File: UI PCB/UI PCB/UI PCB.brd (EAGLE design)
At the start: 160 x 100 mm, 23 parts, among them IC1 MCP23S17SP, IC2 MCP23S17SP, X1 JST-XH-02-PIN-ROUND-PAD, X2 JST-XH-02-PIN-ROUND-PAD, X3 JST-XH-02-PIN-ROUND-PAD, X4 JST-XH-02-PIN-ROUND-PAD, X5 JST-XH-05-PIN-ROUND-PAD, X6 JST-XH-05-PIN-ROUND-PAD, X7 JST-XH-05-PIN-ROUND-PAD, X8 JST-XH-05-PIN-ROUND-PAD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

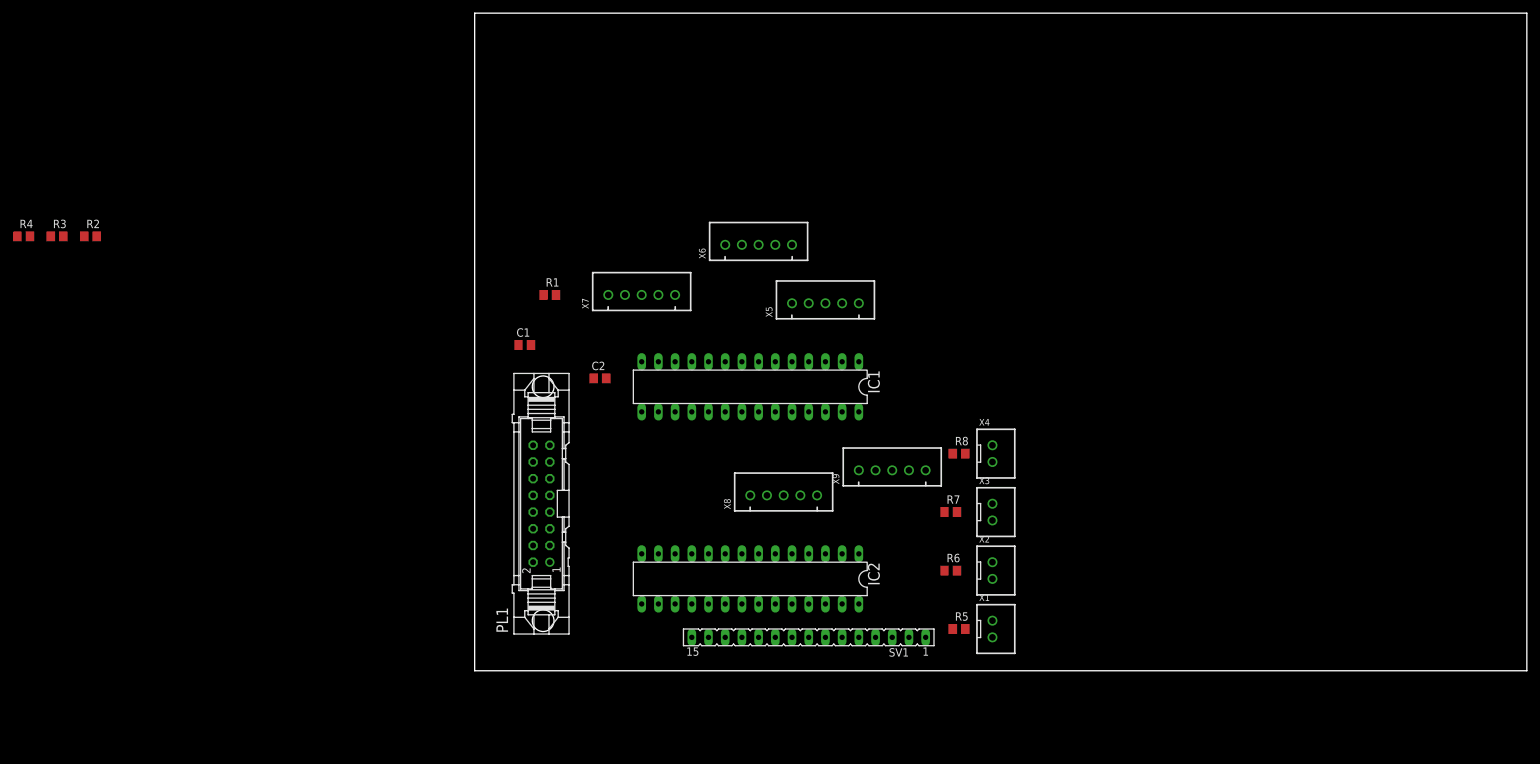
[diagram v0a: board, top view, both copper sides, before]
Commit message: added libraries and a part of the PCB design
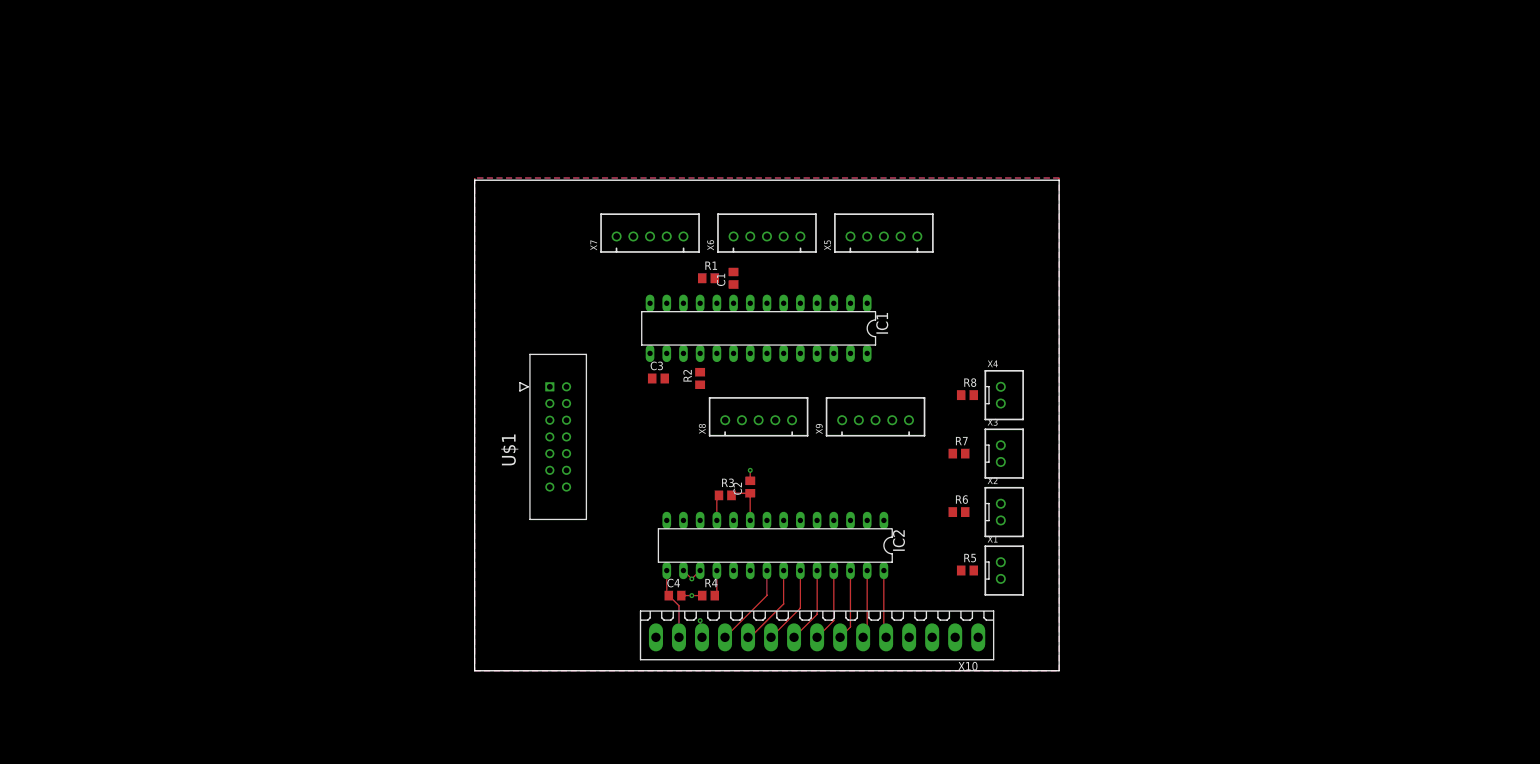
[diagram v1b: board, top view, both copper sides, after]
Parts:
- removed PL1: (no value), con-harting-v:16V
- removed SV1: (no value), con-lsta:FE15
- added C3, C4: (no value), rcl:C0805
- added U$1: 2514-6002UB, 2514-6002UB:3M_2514-6002UB
- added X10: (no value), con-weidmueller-sl35:180G-15
- moved R4 117.6 mm to (35.6, 11.4)
- moved R3 109.0 mm to (38.1, 26.7)
- moved R2 95.2 mm to (34.3, 44.5), turned to 90 degrees
- moved C1 33.3 mm to (39.4, 59.7), turned to 90 degrees
- moved C2 28.2 mm to (41.9, 27.9), turned to 90 degrees
- moved R1 24.3 mm to (35.6, 59.7)
- moved X5 13.5 mm to (62.2, 66.0)
- moved X8 12.0 mm to (43.2, 38.1)
- moved X7 8.98 mm to (26.7, 66.0)
- moved X3 8.98 mm to (80.0, 33.0)
- moved R7 8.98 mm to (73.7, 33.0)
- moved IC1 8.98 mm to (43.2, 52.1)
- moved R5 8.98 mm to (74.9, 15.2)
- moved X1 8.98 mm to (80.0, 15.2)
- moved X2 8.98 mm to (80.0, 24.1)
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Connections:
- removed net A0: IC1.15, IC2.15, PL1.5
- removed net A1: IC1.16, IC2.16, PL1.6
- removed net CLK: PL1.7
- removed net N$16: PL1.16
- new net N$1: U$1.1
- new net N$10: U$1.6
- new net N$11: U$1.8
- new net N$12: U$1.10
- new net N$13: U$1.12
- new net N$14: U$1.14
- new net N$2: U$1.3
- new net N$3: U$1.5
- new net N$4: U$1.7
- new net N$5: U$1.9
- new net N$6: U$1.11
- new net N$7: U$1.13
- new net N$8: U$1.2
- new net N$9: U$1.4
- net 3V3: now also C3.1, C4.1, IC2.15, X10.14; no longer PL1.13, SV1.14
- net 5V: now also X10.15; no longer PL1.14, SV1.15
- net CS1: no longer PL1.10
- net CS2: no longer PL1.11
- net GND: now also C3.2, C4.2, IC1.15, IC1.16, IC1.17, IC2.16, IC2.17, X10.13; no longer PL1.15, SV1.13
- net GPA0: now also X10.12; no longer SV1.12
- net GPA1: now also X10.11; no longer SV1.11
- net GPA2: now also X10.10; no longer SV1.10
- net GPA3: now also X10.9; no longer SV1.9
- net GPA4: now also X10.8; no longer SV1.8
- net GPA5: now also X10.7; no longer SV1.7
- net GPA6: now also X10.6; no longer SV1.6
- net GPA7: now also X10.5; no longer SV1.5
- net GPB4: now also X10.4; no longer SV1.4
- net GPB5: now also X10.3; no longer SV1.3
- net GPB6: now also X10.2; no longer SV1.2
- net GPB7: now also X10.1; no longer SV1.1
- net INTA1: no longer PL1.1
- net INTA2: no longer PL1.3
- net INTB1: no longer PL1.2
- net INTB2: no longer PL1.4
- net MISO: no longer PL1.8
- net MOSI: no longer PL1.9
- net RESET: no longer PL1.12
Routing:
- net 3V3: track 0.00 -> 18.1 mm
- net GPA0: track 0.00 -> 12.8 mm
- net GPA1: track 0.00 -> 12.3 mm
- net GPA2: track 0.00 -> 12.0 mm
- net GPA3: track 0.00 -> 11.6 mm
- net GPA4: track 0.00 -> 11.2 mm
- net GND: track 0.00 -> 11.0 mm, vias 0 -> 4
- net GPA5: track 0.00 -> 10.8 mm
- net GPA6: track 0.00 -> 10.4 mm
- net GPA7: track 0.00 -> 10.3 mm
- net CS2: track 0.00 -> 3.94 mm
- net RESET: track 0.00 -> 3.94 mm
- added copper zone on layer 1, net GND
- added copper zone on layer 16, net GND
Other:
- board size 160 x 100 mm -> 88.9 x 74.6 mm

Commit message: improve the schemetic on the io expanders and add the right header for the stm32 connection
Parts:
- removed C3, C4: (no value), rcl:C0805
- moved C1 77.9 mm to (7.62, -11.4), turned to 0 degrees
- moved R1 72.7 mm to (2.54, -5.08)
- moved R2 64.3 mm to (2.54, -11.4), turned to 0 degrees
- moved X8 3.81 mm to (43.2, 34.3)
- moved X9 3.81 mm to (61.0, 34.3)
- moved IC1 3.59 mm to (45.7, 49.5)
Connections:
- net N$1 renamed OPEN
- removed net N$10: U$1.6
- removed net N$11: U$1.8
- removed net N$12: U$1.10
- removed net N$13: U$1.12
- removed net N$14: U$1.14
- removed net N$2: U$1.3
- removed net N$3: U$1.5
- removed net N$4: U$1.7
- removed net N$5: U$1.9
- removed net N$6: U$1.11
- removed net N$7: U$1.13
- removed net N$8: U$1.2
- removed net N$9: U$1.4
- removed net SCK: IC1.12, IC2.12
- new net CLK: IC1.12, IC2.12, U$1.14
- net 3V3: now also U$1.4; no longer C3.1, C4.1, R1.2, R3.2
- net 5V: now also U$1.3
- net CS1: now also R1.2, U$1.11; no longer R1.1
- net CS2: now also R3.2, U$1.10; no longer R3.1
- net GND: now also R1.1, R3.1, U$1.2; no longer C3.2, C4.2
- net INTA1: now also U$1.8
- net INTA2: now also U$1.5
- net INTB1: now also U$1.7
- net INTB2: now also U$1.6
- net MISO: now also U$1.13
- net MOSI: now also U$1.12
- net RESET: now also U$1.9
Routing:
- net ROTARY_ENC_5_B: track 0.00 -> 20.5 mm
- net 3V3: track 18.1 -> 37.5 mm
- net ROTARY_ENC_4_BUTTON: track 0.00 -> 18.0 mm
- net ROTARY_ENC_4_A: track 0.00 -> 15.1 mm
- net ROTARY_ENC_5_BUTTON: track 0.00 -> 13.0 mm
- net ROTARY_ENC_5_A: track 0.00 -> 12.0 mm
- net ROTARY_ENC_4_B: track 0.00 -> 12.0 mm
- net CS2: track 3.94 -> 0.00 mm
- net GND: track 11.0 -> 9.43 mm
- net GPA1: track 12.3 -> 11.0 mm

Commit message: redesigned PCB
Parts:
- removed X10: (no value), con-weidmueller-sl35:180G-15
- added J1: (no value), SparkFun-Connectors:1X15
- moved X5 42.8 mm to (25.1, 44.7)
- moved X6 41.9 mm to (8.38, 44.7)
- moved X7 40.2 mm to (3.05, 33.5), turned to 270 degrees
- moved IC1 38.7 mm to (20.3, 20.3), turned to 270 degrees
- moved R2 32.4 mm to (26.7, 10.2), turned to 90 degrees
- moved C1 28.4 mm to (12.7, 16.5), turned to 180 degrees
- moved U$1 24.1 mm to (6.35, 20.3)
- moved X9 21.7 mm to (41.9, 44.7)
- moved R5 19.4 mm to (58.4, 5.08), turned to 90 degrees
- moved X1 19.4 mm to (63.5, 5.08), turned to 90 degrees
- moved R1 19.4 mm to (12.7, 11.4)
- moved X2 18.8 mm to (63.5, 15.2), turned to 90 degrees
- moved X8 18.7 mm to (58.7, 44.7)
- moved X3 18.2 mm to (63.5, 25.4), turned to 90 degrees
- moved R8 17.7 mm to (58.4, 35.6), turned to 90 degrees
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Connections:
- net 3V3: now also J1.14, X5.2, X6.2, X7.2, X8.2, X9.2; no longer X10.14, X5.3, X6.3, X7.3, X8.3, X9.3
- net 5V: now also J1.15; no longer X10.15
- net GND: now also J1.13, X5.1, X6.1, X7.1, X8.1, X9.1; no longer X10.13, X5.2, X6.2, X7.2, X8.2, X9.2
- net GPA0: now also J1.12; no longer X10.12
- net GPA1: now also J1.11; no longer X10.11
- net GPA2: now also J1.10; no longer X10.10
- net GPA3: now also J1.9; no longer X10.9
- net GPA4: now also J1.8; no longer X10.8
- net GPA5: now also J1.7; no longer X10.7
- net GPA6: now also J1.6; no longer X10.6
- net GPA7: now also J1.5; no longer X10.5
- net GPB4: now also J1.4; no longer X10.4
- net GPB5: now also J1.3; no longer X10.3
- net GPB6: now also J1.2; no longer X10.2
- net GPB7: now also J1.1; no longer X10.1
- net ROTARY_ENC_1_A: now also X5.5; no longer X5.1
- net ROTARY_ENC_1_B: now also X5.4; no longer X5.5
- net ROTARY_ENC_1_BUTTON: now also X5.3; no longer X5.4
- net ROTARY_ENC_2_A: now also X6.5; no longer X6.1
- net ROTARY_ENC_2_B: now also X6.4; no longer X6.5
- net ROTARY_ENC_2_BUTTON: now also X6.3; no longer X6.4
- net ROTARY_ENC_3_A: now also IC1.8, X7.5; no longer IC1.7, X7.1
- net ROTARY_ENC_3_B: now also IC1.7, X7.4; no longer IC1.8, X7.5
- net ROTARY_ENC_3_BUTTON: now also X7.3; no longer X7.4
- net ROTARY_ENC_4_A: now also X8.5; no longer X8.1
- net ROTARY_ENC_4_B: now also X8.4; no longer X8.5
- net ROTARY_ENC_4_BUTTON: now also X8.3; no longer X8.4
- net ROTARY_ENC_5_A: now also X9.5; no longer X9.1
- net ROTARY_ENC_5_B: now also X9.4; no longer X9.5
- net ROTARY_ENC_5_BUTTON: now also X9.3; no longer X9.4
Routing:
- net 3V3: track 37.5 -> 191.2 mm, vias 0 -> 2
- net 5V: track 0.00 -> 65.2 mm
- net CS1_BUTTON: track 0.00 -> 62.7 mm
- net CS2_BUTTON: track 0.00 -> 57.8 mm
- net CS3_BUTTON: track 0.00 -> 51.2 mm
- net CS4_BUTTON: track 0.00 -> 44.7 mm
- net INTA2: track 0.00 -> 41.7 mm, vias 0 -> 1
- net RESET: track 3.94 -> 44.9 mm
- net ROTARY_ENC_4_A: track 15.1 -> 55.3 mm
- net INTB2: track 0.00 -> 39.8 mm
- net GPB4: track 0.00 -> 39.3 mm
- net ROTARY_ENC_4_B: track 12.0 -> 50.5 mm
- net GPB5: track 0.00 -> 38.3 mm
- net GPB6: track 0.00 -> 37.3 mm
- net GPB7: track 0.00 -> 35.4 mm
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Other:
- board size 88.9 x 74.6 mm -> 67.3 x 50.5 mm

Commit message: put every trace on top layer
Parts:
- moved R1 1.02 mm to (12.7, 10.4)
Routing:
- net 3V3: track 191.2 -> 210.6 mm, vias 2 -> 0
- net INTB2: track 39.8 -> 43.7 mm
- net CS2: track 29.9 -> 31.6 mm, vias 2 -> 0
- net INTA2: vias 1 -> 0
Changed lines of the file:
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@@
 <attribute name="VALUE" x="38.4302" y="34.798" size="1.778" layer="27" ratio="10" rot="R270"/>
 </element>
-<element name="R1" library="rcl" library_urn="urn:adsk.eagle:library:334" package="R0805" package3d_urn="urn:adsk.eagle:package:23553/2" value="4k7" x="12.7" y="11.43" smashed="yes">
-<attribute name="NAME" x="10.541" y="12.7" size="1.27" layer="25"/>
-<attribute name="POPULARITY" value="86" x="66.04" y="-69.85" size="1.778" layer="27" display="off"/>
-<attribute name="SPICEPREFIX" value="R" x="66.04" y="-69.85" size="1.778" layer="27" display="off"/>
+<element name="R1" library="rcl" library_urn="urn:adsk.eagle:library:334" package="R0805" package3d_urn="urn:adsk.eagle:package:23553/2" value="4k7" x="12.7" y="10.414" smashed="yes">
+<attribute name="NAME" x="10.541" y="11.684" size="1.27" layer="25"/>
+<attribute name="POPULARITY" value="86" x="66.04" y="-70.866" size="1.778" layer="27" display="off"/>
+<attribute name="SPICEPREFIX" value="R" x="66.04" y="-70.866" size="1.778" layer="27" display="off"/>
 </element>
 <element name="R2" library="rcl" library_urn="urn:adsk.eagle:library:334" package="R0805" package3d_urn="urn:adsk.eagle:package:23553/2" value="4k7" x="26.67" y="10.16" smashed="yes" rot="R90">
@@
 </polygon>
 <via x="10.16" y="16.002" extent="1-16" drill="0.35"/>
-<via x="10.16" y="10.922" extent="1-16" drill="0.35"/>
 <via x="28.448" y="16.764" extent="1-16" drill="0.35"/>
 <via x="28.702" y="11.43" extent="1-16" drill="0.35"/>
@@
 <via x="34.798" y="44.704" extent="1-16" drill="0.35"/>
 <via x="18.288" y="44.704" extent="1-16" drill="0.35"/>
+<via x="10.16" y="9.906" extent="1-16" drill="0.35"/>
 </signal>
 <signal name="3V3">
@@
 <contactref element="U$1" pad="4"/>
 <contactref element="J1" pad="14"/>
-<wire x1="3.048" y1="36.068" x2="5.842" y2="38.862" width="0.1524" layer="1"/>
+<wire x1="3.048" y1="36.068" x2="3.175" y2="36.195" width="0.1524" layer="1"/>
+<wire x1="3.175" y1="36.195" x2="5.842" y2="38.862" width="0.1524" layer="1"/>
 <wire x1="5.842" y1="38.862" x2="5.842" y2="44.704" width="0.1524" layer="1"/>
 <wire x1="5.842" y1="44.704" x2="6.858" y2="45.72" width="0.1524" layer="1"/>
@@
 <wire x1="55.626" y1="2.794" x2="62.484" y2="2.794" width="0.1524" layer="1"/>
 <wire x1="62.484" y1="2.794" x2="63.5" y2="3.81" width="0.1524" layer="1"/>
-<wire x1="6.35" y1="17.78" x2="7.62" y2="17.78" width="0.1524" layer="1"/>
-<via x="7.62" y="17.78" extent="1-16" drill="0.35"/>
-<wire x1="7.62" y1="17.78" x2="15.24" y2="17.78" width="0.1524" layer="16"/>
-<wire x1="15.24" y1="17.78" x2="16.51" y2="16.51" width="0.1524" layer="16"/>
 <wire x1="16.51" y1="16.51" x2="21.59" y2="16.51" width="0.1524" layer="1"/>
 <wire x1="28.0233125" y1="15.5314" x2="31.5446875" y2="15.5314" width="0.1524" layer="1"/>
@@
 <wire x1="21.59" y1="16.51" x2="22.479" y2="17.399" width="0.1524" layer="1"/>
 <wire x1="32.7" y1="16.51" x2="33.97" y2="15.24" width="0.1524" layer="1"/>
-<wire x1="33.97" y1="15.24" x2="34.036" y2="15.24" width="0.1524" layer="1"/>
-<via x="34.036" y="15.24" extent="1-16" drill="0.35"/>
-<wire x1="34.0106" y1="14.3382375" x2="34.0106" y2="13.6017625" width="0.1524" layer="16"/>
-<wire x1="34.0106" y1="13.6017625" x2="34.5313625" y2="13.081" width="0.1524" layer="16"/>
-<wire x1="34.036" y1="15.24" x2="34.036" y2="14.3636375" width="0.1524" layer="16"/>
-<wire x1="34.036" y1="14.3636375" x2="34.0106" y2="14.3382375" width="0.1524" layer="16"/>
-<wire x1="43.18" y1="4.4323625" x2="43.18" y2="3.81" width="0.1524" layer="16"/>
-<wire x1="41.6306" y1="5.9817625" x2="43.18" y2="4.4323625" width="0.1524" layer="16"/>
-<wire x1="34.5313625" y1="13.081" x2="35.8266375" y2="13.081" width="0.1524" layer="16"/>
-<wire x1="35.8266375" y1="13.081" x2="41.6306" y2="7.2770375" width="0.1524" layer="16"/>
-<wire x1="41.6306" y1="7.2770375" x2="41.6306" y2="5.9817625" width="0.1524" layer="16"/>
+<wire x1="33.97" y1="15.24" x2="34.0106" y2="15.1994" width="0.1524" layer="1"/>
+<wire x1="34.0106" y1="15.1994" x2="34.0106" y2="13.6017625" width="0.1524" layer="1"/>
+<wire x1="34.0106" y1="13.6017625" x2="34.6075625" y2="13.0048" width="0.1524" layer="1"/>
+<wire x1="46.6986" y1="11.8546875" x2="46.6986" y2="10.3653125" width="0.1524" layer="1"/>
+<wire x1="46.6986" y1="10.3653125" x2="46.5646875" y2="10.2314" width="0.1524" layer="1"/>
+<wire x1="43.18" y1="4.4323625" x2="43.18" y2="3.81" width="0.1524" layer="1"/>
+<wire x1="44.7294" y1="5.9817625" x2="43.18" y2="4.4323625" width="0.1524" layer="1"/>
+<wire x1="46.5646875" y1="10.2314" x2="45.0181125" y2="10.2314" width="0.1524" layer="1"/>
+<wire x1="45.5484875" y1="13.0048" x2="46.6986" y2="11.8546875" width="0.1524" layer="1"/>
+<wire x1="45.0181125" y1="10.2314" x2="44.7294" y2="9.9426875" width="0.1524" layer="1"/>
+<wire x1="44.7294" y1="9.9426875" x2="44.7294" y2="5.9817625" width="0.1524" layer="1"/>
+<wire x1="34.6075625" y1="13.0048" x2="45.5484875" y2="13.0048" width="0.1524" layer="1"/>
+<wire x1="6.35" y1="17.78" x2="4.826" y2="19.304" width="0.1524" layer="1"/>
+<wire x1="4.826" y1="25.269075" x2="2.0574" y2="28.037675" width="0.1524" layer="1"/>
+<wire x1="2.0574" y1="28.037675" x2="2.0574" y2="33.938325" width="0.1524" layer="1"/>
+<wire x1="3.175" y1="35.055925" x2="3.175" y2="36.195" width="0.1524" layer="1"/>
+<wire x1="2.0574" y1="33.938325" x2="3.175" y2="35.055925" width="0.1524" layer="1"/>
+<wire x1="4.826" y1="19.304" x2="4.826" y2="25.269075" width="0.1524" layer="1"/>
 </signal>
 <signal name="RESET">
@@
 <contactref element="IC1" pad="11"/>
 <contactref element="U$1" pad="11"/>
-<wire x1="16.51" y1="11.43" x2="13.716" y2="11.43" width="0.1524" layer="1"/>
-<wire x1="13.716" y1="11.43" x2="13.65" y2="11.43" width="0.1524" layer="1"/>
 <wire x1="3.81" y1="7.62" x2="5.08" y2="8.89" width="0.1524" layer="1"/>
-<wire x1="11.176" y1="8.89" x2="13.716" y2="11.43" width="0.1524" layer="1"/>
-<wire x1="5.08" y1="8.89" x2="11.176" y2="8.89" width="0.1524" layer="1"/>
+<wire x1="13.65" y1="10.414" x2="13.683" y2="10.447" width="0.1524" layer="1"/>
+<wire x1="13.683" y1="10.447" x2="14.666" y2="11.43" width="0.1524" layer="1"/>
+<wire x1="14.666" y1="11.43" x2="16.51" y2="11.43" width="0.1524" layer="1"/>
+<wire x1="12.126" y1="8.89" x2="13.65" y2="10.414" width="0.1524" layer="1"/>
+<wire x1="5.08" y1="8.89" x2="12.126" y2="8.89" width="0.1524" layer="1"/>
 </signal>
 <signal name="INTA1">
@@
 <wire x1="3.81" y1="15.24" x2="5.03888125" y2="15.24" width="0.1524" layer="1"/>
 <wire x1="5.03888125" y1="15.24" x2="5.96598125" y2="14.3129" width="0.1524" layer="1"/>
-<wire x1="37.592" y1="17.78" x2="38.862" y2="16.51" width="0.1524" layer="1"/>
-<via x="38.862" y="16.51" extent="1-16" drill="0.35"/>
-<wire x1="38.862" y1="16.51" x2="43.18" y2="16.51" width="0.1524" layer="16"/>
-<wire x1="10.87628125" y1="17.78" x2="37.592" y2="17.78" width="0.1524" layer="1"/>
 <wire x1="7.40918125" y1="14.3129" x2="10.87628125" y2="17.78" width="0.1524" layer="1"/>
 <wire x1="5.96598125" y1="14.3129" x2="7.40918125" y2="14.3129" width="0.1524" layer="1"/>
+<wire x1="41.91" y1="17.78" x2="43.18" y2="16.51" width="0.1524" layer="1"/>
+<wire x1="10.87628125" y1="17.78" x2="41.91" y2="17.78" width="0.1524" layer="1"/>
 </signal>
 <signal name="INTB2">
@@
 <contactref element="U$1" pad="6"/>
 <wire x1="6.35" y1="15.24" x2="9.271" y2="18.161" width="0.1524" layer="1"/>
-<wire x1="38.989" y1="18.161" x2="43.18" y2="13.97" width="0.1524" layer="1"/>
-<wire x1="9.271" y1="18.161" x2="38.989" y2="18.161" width="0.1524" layer="1"/>
+<wire x1="9.271" y1="18.161" x2="38.862" y2="18.161" width="0.1524" layer="1"/>
+<wire x1="38.862" y1="18.161" x2="38.989" y2="18.161" width="0.1524" layer="1"/>
+<wire x1="44.7294" y1="16.8782375" x2="44.7294" y2="16.1417625" width="0.1524" layer="1"/>
+<wire x1="38.989" y1="18.161" x2="43.4466375" y2="18.161" width="0.1524" layer="1"/>
+<wire x1="43.4466375" y1="18.161" x2="44.7294" y2="16.8782375" width="0.1524" layer="1"/>
+<wire x1="44.7294" y1="16.1417625" x2="43.18" y2="14.5923625" width="0.1524" layer="1"/>
+<wire x1="43.18" y1="14.5923625" x2="43.18" y2="13.97" width="0.1524" layer="1"/>
 </signal>
 <signal name="GPA0">
@@
 <contactref element="U$1" pad="10"/>
 <wire x1="35.56" y1="11.43" x2="32.7" y2="11.43" width="0.1524" layer="1"/>
-<wire x1="6.35" y1="10.16" x2="11.0384" y2="10.16" width="0.1524" layer="1"/>
-<wire x1="11.0384" y1="10.16" x2="11.176" y2="10.0224" width="0.1524" layer="1"/>
-<via x="11.176" y="10.0224" extent="1-16" drill="0.35"/>
-<wire x1="14.07605" y1="10.0429" x2="14.05555" y2="10.0224" width="0.1524" layer="16"/>
-<wire x1="14.05555" y1="10.0224" x2="11.176" y2="10.0224" width="0.1524" layer="16"/>
-<via x="14.07605" y="10.0429" extent="1-16" drill="0.35"/>
 <wire x1="32.5232875" y1="11.43" x2="32.7" y2="11.43" width="0.1524" layer="1"/>
-<wire x1="31.2631875" y1="10.1699" x2="32.5232875" y2="11.43" width="0.1524" layer="1"/>
-<wire x1="31.2631875" y1="10.1699" x2="14.20305" y2="10.1699" width="0.1524" layer="1"/>
-<wire x1="14.07605" y1="10.0429" x2="14.20305" y2="10.1699" width="0.1524" layer="1"/>
+<wire x1="6.35" y1="10.16" x2="7.0612" y2="10.8712" width="0.1524" layer="1"/>
+<wire x1="7.0612" y1="10.8712" x2="9.52425625" y2="10.8712" width="0.1524" layer="1"/>
+<wire x1="9.52425625" y1="10.8712" x2="11.04825625" y2="12.3952" width="0.1524" layer="1"/>
+<wire x1="21.2471625" y1="12.3952" x2="23.4823625" y2="10.16" width="0.1524" layer="1"/>
+<wire x1="23.4823625" y1="10.16" x2="31.2532875" y2="10.16" width="0.1524" layer="1"/>
+<wire x1="11.04825625" y1="12.3952" x2="21.2471625" y2="12.3952" width="0.1524" layer="1"/>
+<wire x1="31.2532875" y1="10.16" x2="32.5232875" y2="11.43" width="0.1524" layer="1"/>
 </signal>
 <signal name="OPEN">
